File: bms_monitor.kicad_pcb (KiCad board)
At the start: 2 copper layers, 115 x 65 mm, 244 parts, among them CN1 10nF, CN10 10nF, CN11 10nF, CN12 10nF, CN13 10nF, CN14 10nF, CN2 10nF, CN3 10nF, CN4 10nF, CN5 10nF, CN6 10nF, CN7 10nF, CN8 10nF, CN9 10nF, J1 Conn_01x02, J10 TEMP0, J11 TEMP1, J12 DIRECT_SPI, J13 Conn_ARM_JTAG_SWD_10, J2 Conn_01x02, J3 Conn_01x02, J4 Conn_01x02, J5 CELLS, J6 TEMP0, J7 TEMP1, J8 DIRECT_SPI, J9 CELLS, Q1 NSV1C201MZ4, Q2 NSV1C201MZ4, U1 STM32L432KBUx, U10 CD74HC4067SM, U11 MP4541, U12 SM91502ALA, U13 SM91502ALA, U14 SM91502ALA, U3 DSC61XX, U4 TFBS4652, U5 LTC6811-1, U6 CD74HC4067SM, U7 MP4541, U8 SM91502ALA, U9 LTC6811-1

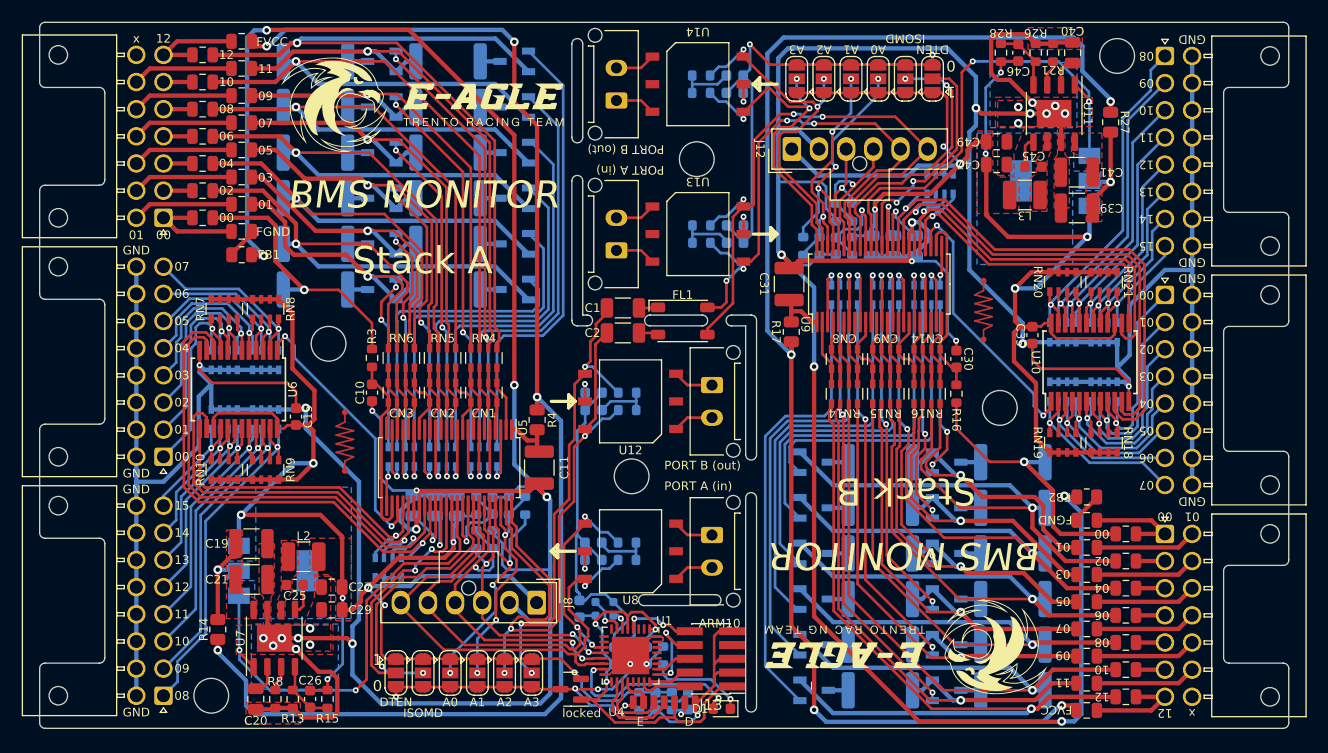
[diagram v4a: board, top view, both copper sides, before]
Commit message: added different VDD pin for external supply
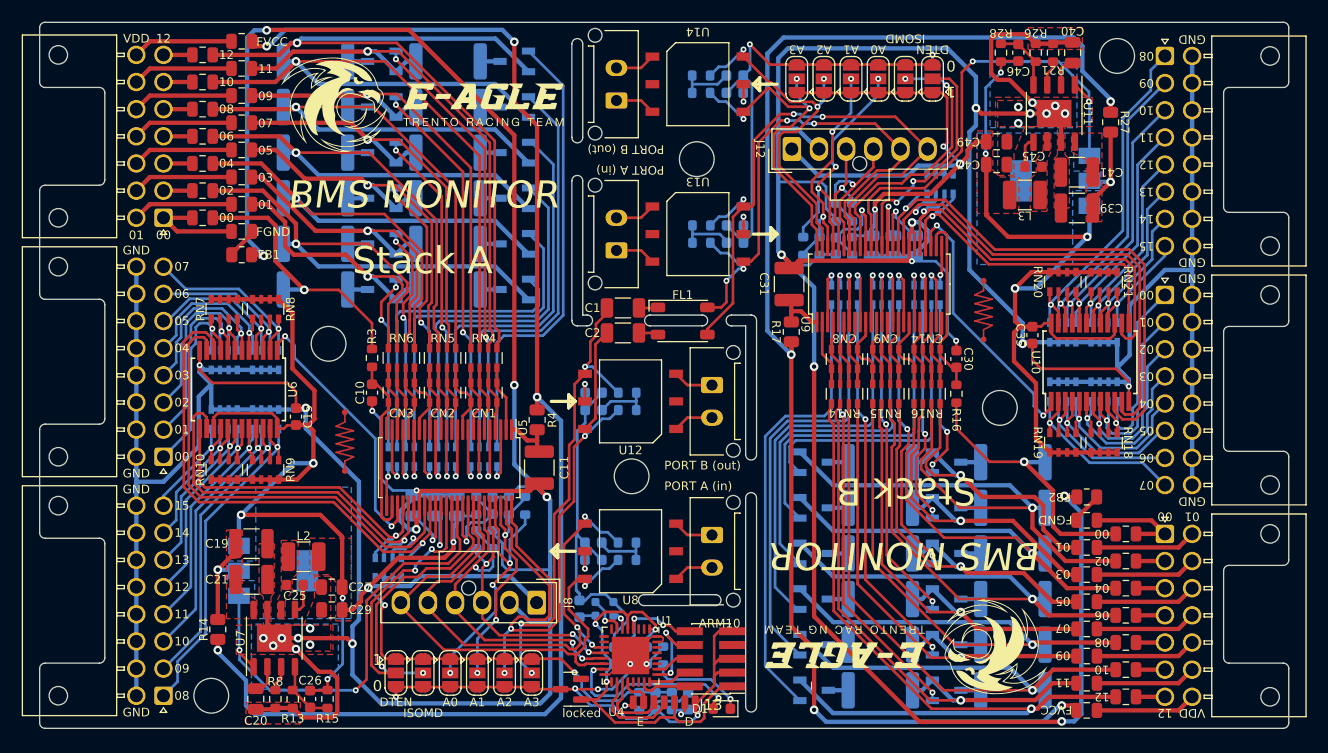
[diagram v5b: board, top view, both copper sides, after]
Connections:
- Fa13 pad 2: Net-(J5-Pin_7) -> Net-(J5-Pin_14)
- Fb3 pad 2: Net-(J9-Pin_7) -> Net-(J9-Pin_14)
- J5 pad 14: unconnected-(J5-Pin_14-Pad14) -> Net-(J5-Pin_14)
- J9 pad 14: unconnected-(J9-Pin_14-Pad14) -> Net-(J9-Pin_14)
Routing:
- net Net-(J9-Pin_14): track 0.00 -> 9.28 mm
- net Net-(J5-Pin_14): track 0.00 -> 9.28 mm
- net Net-(J9-Pin_7): track 9.44 -> 2.66 mm
- net Net-(J5-Pin_7): track 9.44 -> 2.66 mm
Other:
- board text added: "Short to VDD=CC12"
- board text added: "VDD"
- board text removed: "x"
- board text removed: "xx"
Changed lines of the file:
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@@
   (net 137 "Net-(J5-Pin_13)")
   (net 138 "Net-(J5-Pin_7)")
-  (net 139 "unconnected-(J5-Pin_14-Pad14)")
-  (net 140 "unconnected-(J9-Pin_14-Pad14)")
+  (net 139 "Net-(J5-Pin_14)")
+  (net 140 "Net-(J9-Pin_14)")
   (net 141 "/StackB/IBIAS_2")
   (net 142 "/StackB/ICMP_2")
@@
       (net 137 "Net-(J5-Pin_13)") (pinfunction "Pin_13") (pintype "passive"))
     (pad "14" thru_hole circle (at 2.5 15 180) (size 1.7 1.7) (drill 1.2) (layers "*.Cu" "*.Mask")
-      (net 139 "unconnected-(J5-Pin_14-Pad14)") (pinfunction "Pin_14") (pintype "passive+no_connect"))
+      (net 139 "Net-(J5-Pin_14)") (pinfunction "Pin_14") (pintype "passive"))
     (model "${KICAD6_3DMODEL_DIR}/Connector_Molex.3dshapes/Molex_Nano-Fit_105314-xx14_2x07_P2.50mm_Horizontal.wrl"
       (offset (xyz 0 0 0))
@@
       (net 233 "/StackA/VDD") (pintype "passive"))
     (pad "2" smd roundrect (at 0.9375 0 180) (size 0.975 1.4) (layers "F.Cu" "F.Paste" "F.Mask") (roundrect_rratio 0.25)
-      (net 138 "Net-(J5-Pin_7)") (pintype "passive"))
+      (net 139 "Net-(J5-Pin_14)") (pintype "passive"))
     (model "${KICAD6_3DMODEL_DIR}/Fuse.3dshapes/Fuse_0805_2012Metric.wrl"
       (offset (xyz 0 0 0))
@@
       (net 120 "Net-(J9-Pin_13)") (pinfunction "Pin_13") (pintype "passive"))
     (pad "14" thru_hole circle (at 2.5 15) (size 1.7 1.7) (drill 1.2) (layers "*.Cu" "*.Mask")
-      (net 140 "unconnected-(J9-Pin_14-Pad14)") (pinfunction "Pin_14") (pintype "passive+no_connect"))
+      (net 140 "Net-(J9-Pin_14)") (pinfunction "Pin_14") (pintype "passive"))
     (model "${KICAD6_3DMODEL_DIR}/Connector_Molex.3dshapes/Molex_Nano-Fit_105314-xx14_2x07_P2.50mm_Horizontal.wrl"
       (offset (xyz 0 0 0))
@@
       (net 234 "/StackB/VDD") (pintype "passive"))
     (pad "2" smd roundrect (at 0.9375 0) (size 0.975 1.4) (layers "F.Cu" "F.Paste" "F.Mask") (roundrect_rratio 0.25)
-      (net 113 "Net-(J9-Pin_7)") (pintype "passive"))
+      (net 140 "Net-(J9-Pin_14)") (pintype "passive"))
     (model "${KICAD6_3DMODEL_DIR}/Fuse.3dshapes/Fuse_0805_2012Metric.wrl"
       (offset (xyz 0 0 0))
@@
   (gr_line (start 123.35 119.25) (end 123.35 125.8)
     (stroke (width 0.15) (type solid)) (layer "B.SilkS"))
+  (gr_line (start 98.9 63.7) (end 90.3 63.7)
+    (stroke (width 0.15) (type default)) (layer "B.SilkS"))
   (gr_line locked (start 149.4 121.55) (end 161.15 121.55)
     (stroke (width 0.15) (type solid)) (layer "B.SilkS"))
@@
   (gr_line (start 120.65 91.55) (end 120.65 92.3)
     (stroke (width 0.15) (type solid)) (layer "B.SilkS"))
+  (gr_line (start 184.85 124.9) (end 184.7 125.4)
+    (stroke (width 0.15) (type default)) (layer "B.SilkS"))
   (gr_line locked (start 125.6 75.95) (end 113.85 75.95)
     (stroke (width 0.15) (type solid)) (layer "B.SilkS"))
@@
   (gr_line (start 123.35 126.05) (end 140.15 126.05)
     (stroke (width 0.15) (type solid)) (layer "B.SilkS"))
+  (gr_line (start 184.2 124.9) (end 185.5 124.9)
+    (stroke (width 0.15) (type default)) (layer "B.SilkS"))
+  (gr_line (start 90.8 64.2) (end 89.5 64.2)
+    (stroke (width 0.15) (type default)) (layer "B.SilkS"))
   (gr_line (start 159 98.9) (end 159.4 97.3)
     (stroke (width 0.15) (type solid)) (layer "B.SilkS"))
@@
   (gr_line locked (start 149.4 117.35) (end 161.15 117.35)
     (stroke (width 0.15) (type solid)) (layer "B.SilkS"))
+  (gr_line (start 90.15 64.2) (end 90.3 63.7)
+    (stroke (width 0.15) (type default)) (layer "B.SilkS"))
   (gr_line (start 152.4 97.3) (end 151.4 97.3)
     (stroke (width 0.15) (type solid)) (layer "B.SilkS"))
@@
   (gr_line (start 118.4 90.2) (end 118 91.8)
     (stroke (width 0.15) (type solid)) (layer "B.SilkS"))
+  (gr_line (start 176.1 125.4) (end 184.7 125.4)
+    (stroke (width 0.15) (type default)) (layer "B.SilkS"))
   (gr_line (start 156.2 98.1) (end 156.6 98.9)
     (stroke (width 0.15) (type solid)) (layer "B.SilkS"))
@@
     (effects (font (size 2 2) (thickness 0.3)) (justify mirror))
   )
+  (gr_text "Short to VDD=CC12" (at 176 125.5 180) (layer "B.SilkS")
+    (effects (font (size 0.8 0.8) (thickness 0.12)) (justify left bottom mirror))
+  )
+  (gr_text "Short to VDD=CC12" (at 99 63.6) (layer "B.SilkS")
+    (effects (font (size 0.8 0.8) (thickness 0.12)) (justify left bottom mirror))
+  )
   (gr_text "10" (at 174.05 122 -180) (layer "B.SilkS")
     (effects (font (size 0.8 0.8) (thickness 0.12)) (justify mirror))
@@
     (effects (font (size 0.8 0.8) (thickness 0.12)) (justify mirror))
   )
-  (gr_text "xx" (at 87.15 65) (layer "B.SilkS")
+  (gr_text "VDD" (at 86.8 65) (layer "B.SilkS")
     (effects (font (size 0.8 0.8) (thickness 0.12)) (justify mirror))
   )
@@
     (effects (font (size 0.8 0.8) (thickness 0.12)) (justify mirror))
   )
-  (gr_text "xx" (at 187.85 124.1 -180) (layer "B.SilkS")
+  (gr_text "VDD" (at 188.2 124.1 180) (layer "B.SilkS")
     (effects (font (size 0.8 0.8) (thickness 0.12)) (justify mirror))
   )
@@
     (effects (font (size 0.8 0.8) (thickness 0.12)))
   )
-  (gr_text "x" (at 186.1 125.6 -180) (layer "F.SilkS")
+  (gr_text "VDD" (at 186.1 125.6 180) (layer "F.SilkS")
     (effects (font (size 0.8 0.8) (thickness 0.12)))
   )
@@
     (effects (font (size 0.8 0.8) (thickness 0.12)))
   )
-  (gr_text "x" (at 88.9 63.5) (layer "F.SilkS")
+  (gr_text "VDD" (at 88.9 63.5) (layer "F.SilkS")
     (effects (font (size 0.8 0.8) (thickness 0.12)))
   )
@@
   (segment (start 141.25 122.95) (end 134.25 122.95) (width 0.25) (layer "B.Cu") (net 112))
   (segment (start 133.2 124) (end 131.151471 124) (width 0.25) (layer "B.Cu") (net 112))
-  (segment (start 177.3375 125.35) (end 182.35 125.35) (width 0.4) (layer "F.Cu") (net 113))
   (segment (start 183.6 124.1) (end 180.9375 124.1) (width 0.4) (layer "F.Cu") (net 113))
-  (segment (start 182.35 125.35) (end 183.6 124.1) (width 0.4) (layer "F.Cu") (net 113))
   (segment (start 183.6 121.6) (end 180.9375 121.6) (width 0.4) (layer "F.Cu") (net 114))
   (segment (start 183.6 119.1) (end 180.9375 119.1) (width 0.4) (layer "F.Cu") (net 115))
@@
   (segment (start 88.9 67.5) (end 90.15 66.25) (width 0.4) (layer "F.Cu") (net 137))
   (segment (start 90.15 66.25) (end 97.6625 66.25) (width 0.4) (layer "F.Cu") (net 137))
-  (segment (start 92.65 63.75) (end 91.4 65) (width 0.4) (layer "F.Cu") (net 138))
   (segment (start 91.4 65) (end 94.0625 65) (width 0.4) (layer "F.Cu") (net 138))
-  (segment (start 97.6625 63.75) (end 92.65 63.75) (width 0.4) (layer "F.Cu") (net 138))
+  (segment (start 97.6625 63.75) (end 90.15 63.75) (width 0.4) (layer "F.Cu") (net 139))
+  (segment (start 90.15 63.75) (end 88.9 65) (width 0.4) (layer "F.Cu") (net 139))
+  (segment (start 184.85 125.35) (end 186.1 124.1) (width 0.4) (layer "F.Cu") (net 140))
+  (segment (start 177.3375 125.35) (end 184.85 125.35) (width 0.4) (layer "F.Cu") (net 140))
   (segment (start 153.861484 77.242655) (end 153.233128 77.871011) (width 0.25) (layer "F.Cu") (net 141))
   (segment (start 153.55 82.6) (end 153.55 80.549135) (width 0.25) (layer "F.Cu") (net 141))

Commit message: fixed enable mux
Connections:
- U10 pad 15: /StackB/VCC -> /StackB/GND
- U6 pad 15: +5V -> GND
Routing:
- net +5V: track 161.0 -> 152.9 mm
- net /StackB/VCC: track 145.7 -> 137.5 mm
- net /StackB/GND: track 364.9 -> 369.1 mm
- net GND: track 425.5 -> 429.7 mm
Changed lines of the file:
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@@
       (net 217 "/StackB/MUX_A2") (pinfunction "S2") (pintype "input"))
     (pad "15" smd rect (at 3.6 2.275 90) (size 1.75 0.45) (layers "F.Cu" "F.Paste" "F.Mask")
-      (net 285 "/StackB/VCC") (pinfunction "~{E}") (pintype "input"))
+      (net 31 "/StackB/GND") (pinfunction "~{E}") (pintype "input"))
     (pad "16" smd rect (at 3.6 1.625 90) (size 1.75 0.45) (layers "F.Cu" "F.Paste" "F.Mask")
       (net 110 "Net-(CN13-R1.2)") (pinfunction "I15") (pintype "passive"))
@@
       (net 208 "/StackA/MUX_A2") (pinfunction "S2") (pintype "input"))
     (pad "15" smd rect (at 3.6 2.275 270) (size 1.75 0.45) (layers "F.Cu" "F.Paste" "F.Mask")
-      (net 10 "+5V") (pinfunction "~{E}") (pintype "input"))
+      (net 7 "GND") (pinfunction "~{E}") (pintype "input"))
     (pad "16" smd rect (at 3.6 1.625 270) (size 1.75 0.45) (layers "F.Cu" "F.Paste" "F.Mask")
       (net 73 "Net-(CN7-R1.2)") (pinfunction "I15") (pintype "passive"))
@@
   (segment locked (start 129.3005 123.332142) (end 129.368358 123.4) (width 0.25) (layer "F.Cu") (net 7))
   (segment locked (start 137.25 118.55) (end 137.4 118.7) (width 0.15) (layer "F.Cu") (net 7))
+  (segment (start 96.025 95.325) (end 95.9 95.2) (width 0.25) (layer "F.Cu") (net 7))
   (segment (start 140.35 125.568835) (end 140.35 124.6) (width 0.25) (layer "F.Cu") (net 7))
   (segment (start 142.6 120.6) (end 143.75 120.6) (width 0.25) (layer "F.Cu") (net 7))
@@
   (segment (start 114.8 105.1) (end 114.7 105.1) (width 0.25) (layer "F.Cu") (net 7))
   (segment locked (start 136.8375 118.55) (end 137.25 118.55) (width 0.15) (layer "F.Cu") (net 7))
+  (segment (start 96.025 99.4) (end 96.025 95.325) (width 0.25) (layer "F.Cu") (net 7))
   (segment locked (start 132.45 122.05) (end 134.2 120.3) (width 0.15) (layer "F.Cu") (net 7))
   (segment (start 104.2 126) (end 106.948528 126) (width 0.4) (layer "F.Cu") (net 7))
@@
   (segment (start 127.9875 120.6) (end 125.3 120.6) (width 0.25) (layer "F.Cu") (net 10))
   (segment (start 107.85 114.95) (end 107.85 114) (width 0.25) (layer "F.Cu") (net 10))
-  (segment (start 96.4 98) (end 101.4 98) (width 0.25) (layer "F.Cu") (net 10))
   (segment (start 103.2745 93.8745) (end 105.3 95.9) (width 0.4) (layer "F.Cu") (net 10))
   (segment (start 118.099 109.866063) (end 118.099 110.470867) (width 0.4) (layer "F.Cu") (net 10))
@@
   (segment (start 104.9 123.525) (end 106.45 123.525) (width 0.25) (layer "F.Cu") (net 10))
   (segment (start 102 87.5) (end 103.2745 88.7745) (width 0.4) (layer "F.Cu") (net 10))
-  (segment (start 101.875 98.475) (end 101.875 99.4) (width 0.25) (layer "F.Cu") (net 10))
   (segment (start 105.3 98.525) (end 104.75 99.075) (width 0.4) (layer "F.Cu") (net 10))
   (segment (start 102.8 99.1) (end 103.575 99.1) (width 0.25) (layer "F.Cu") (net 10))
   (segment (start 117.95 109.717063) (end 118.099 109.866063) (width 0.25) (layer "F.Cu") (net 10))
-  (segment (start 101.4 98) (end 101.875 98.475) (width 0.25) (layer "F.Cu") (net 10))
   (segment (start 95.8 87.5) (end 102 87.5) (width 0.4) (layer "F.Cu") (net 10))
-  (segment (start 96.025 99.4) (end 96.025 98.375) (width 0.25) (layer "F.Cu") (net 10))
   (segment (start 103.7 104.1) (end 105.2 102.6) (width 0.4) (layer "F.Cu") (net 10))
   (segment (start 95.8 104.1) (end 102 104.1) (width 0.4) (layer "F.Cu") (net 10))
@@
   (segment (start 112.8 120.6) (end 125.3 120.6) (width 0.25) (layer "F.Cu") (net 10))
   (segment (start 117.269867 111.3) (end 113.017864 111.3) (width 0.4) (layer "F.Cu") (net 10))
-  (segment (start 96.025 98.375) (end 96.4 98) (width 0.25) (layer "F.Cu") (net 10))
   (segment (start 105.2 99.6) (end 104.675 99.075) (width 0.4) (layer "F.Cu") (net 10))
   (segment (start 111.9 120.6) (end 112.8 120.6) (width 0.25) (layer "F.Cu") (net 10))
@@
   (segment (start 169.3 67.3) (end 171.4 69.4) (width 0.4) (layer "F.Cu") (net 31))
   (segment (start 171.4 69.4) (end 172.4 70.4) (width 0.4) (layer "F.Cu") (net 31))
+  (segment (start 178.975 89.7) (end 178.975 93.775) (width 0.25) (layer "F.Cu") (net 31))
   (segment (start 170.5245 91.575) (end 170.4995 91.6) (width 0.4) (layer "F.Cu") (net 31))
+  (segment (start 178.975 93.775) (end 179.1 93.9) (width 0.25) (layer "F.Cu") (net 31))
   (segment (start 170.8 63.1) (end 168.051472 63.1) (width 0.4) (layer "F.Cu") (net 31))
   (segment (start 160.2 81.3) (end 160.4 81.3) (width 0.25) (layer "F.Cu") (net 31))
@@
   (segment (start 173 101.6) (end 171.7255 100.3255) (width 0.4) (layer "F.Cu") (net 285))
   (segment (start 169.7 90.575) (end 170.25 90.025) (width 0.4) (layer "F.Cu") (net 285))
-  (segment (start 178.975 90.725) (end 178.6 91.1) (width 0.25) (layer "F.Cu") (net 285))
   (segment (start 166.2 73) (end 165.425 73.775) (width 0.4) (layer "F.Cu") (net 285))
   (segment (start 173.125 89.7) (end 172.5 89.7) (width 0.25) (layer "F.Cu") (net 285))
   (segment (start 171.7255 95.2255) (end 169.7 93.2) (width 0.4) (layer "F.Cu") (net 285))
   (segment (start 171.3 85) (end 169.8 86.5) (width 0.4) (layer "F.Cu") (net 285))
-  (segment (start 178.975 89.7) (end 178.975 90.725) (width 0.25) (layer "F.Cu") (net 285))
   (segment (start 169.8 89.5) (end 170.325 90.025) (width 0.4) (layer "F.Cu") (net 285))
   (segment (start 171.425 90) (end 171.4 90.025) (width 0.25) (layer "F.Cu") (net 285))
@@
   (segment (start 171.7255 100.3255) (end 171.7255 95.2255) (width 0.4) (layer "F.Cu") (net 285))
   (segment (start 169.15 81.75) (end 167.15 79.75) (width 0.4) (layer "F.Cu") (net 285))
-  (segment (start 173.6 91.1) (end 173.125 90.625) (width 0.25) (layer "F.Cu") (net 285))
   (segment (start 163.55 73.086924) (end 163.55 68.95) (width 0.25) (layer "F.Cu") (net 285))
   (segment (start 167.15 73) (end 166.2 73) (width 0.4) (layer "F.Cu") (net 285))
@@
   (segment (start 179.2 85) (end 173 85) (width 0.4) (layer "F.Cu") (net 285))
   (segment (start 163.1 68.5) (end 162.2 68.5) (width 0.25) (layer "F.Cu") (net 285))
-  (segment (start 173.125 90.625) (end 173.125 89.7) (width 0.25) (layer "F.Cu") (net 285))
   (segment (start 179.2 101.6) (end 173 101.6) (width 0.4) (layer "F.Cu") (net 285))
   (segment (start 167.15 74.15) (end 167.15 75.1) (width 0.25) (layer "F.Cu") (net 285))
@@
   (segment (start 172.2 90) (end 171.425 90) (width 0.25) (layer "F.Cu") (net 285))
   (segment (start 169.7 93.2) (end 169.7 90.575) (width 0.4) (layer "F.Cu") (net 285))
-  (segment (start 178.6 91.1) (end 173.6 91.1) (width 0.25) (layer "F.Cu") (net 285))
   (via (at 168.5 66.6255) (size 0.55) (drill 0.25) (layers "F.Cu" "B.Cu") (net 285))
   (via (at 163.205065 73.431859) (size 0.55) (drill 0.25) (layers "F.Cu" "B.Cu") (net 285))
